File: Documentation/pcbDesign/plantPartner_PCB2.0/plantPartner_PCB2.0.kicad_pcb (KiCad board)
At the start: 2 copper layers, 85.3 x 70.5 mm, 60 parts, among them IC1 MPM3610, J1 Conn_01x04, J10 Screw_Terminal_01x02, J11 Conn_01x02, J16 Conn_01x04, J17 Conn_01x03, J2 Conn_01x04, J20 Conn_02x04_Top_Bottom, J21 Conn_01x04, J22 Conn_01x04, J23 Conn_01x01, J24 Conn_01x03, J25 Conn_01x03, J26 Conn_01x01, J27 Conn_01x01, J28 Conn_01x01, J29 Conn_01x02, J3 Conn_01x04, J30 Screw_Terminal_01x02, J4 Screw_Terminal, J5 Conn_01x02, J6 Barrel_Jack, J7 Screw_Terminal_01x02, J8 Conn_02x04_Top_Bottom, J9 Screw_Terminal_01x02, Q1 AO3400A, Q2 AO3400A, Q4 AO3400A, U2 MAX485, U3 ESP32-DEVKIT-V1

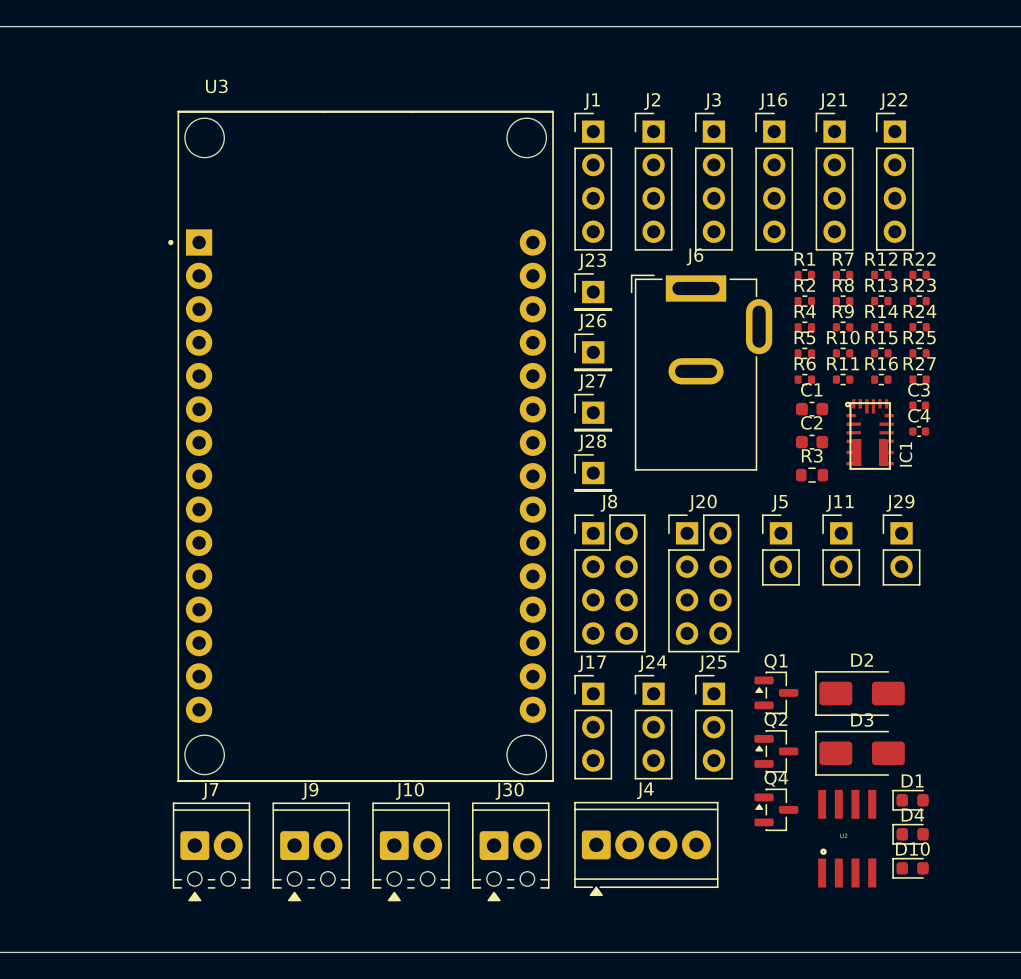
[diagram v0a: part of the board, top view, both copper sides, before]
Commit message: Cleaning up MOSFET circuits
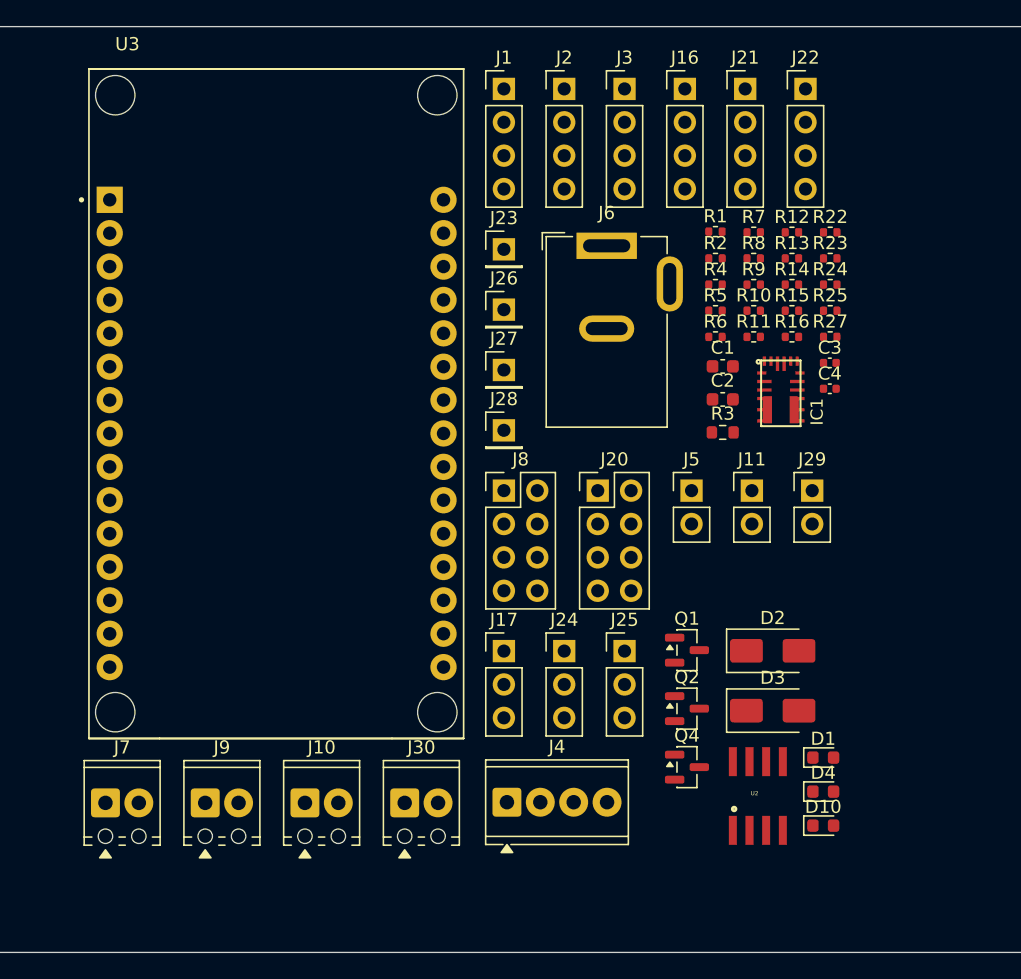
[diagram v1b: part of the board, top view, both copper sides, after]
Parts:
- moved R1 7.56 mm to (131.5, 50.4)
- moved U3 7.54 mm to (98.1, 63.5)
- moved C1 7.54 mm to (132.0, 60.7)
- moved C2 7.54 mm to (132.0, 63.2)
- moved C3 7.54 mm to (140.2, 60.4)
- moved C4 7.54 mm to (140.2, 62.4)
- moved D1 7.54 mm to (139.7, 90.4)
- moved D10 7.54 mm to (139.7, 95.6)
- moved D2 7.54 mm to (135.8, 82.3)
- moved D3 7.54 mm to (135.8, 86.8)
- moved D4 7.54 mm to (139.7, 93.0)
- moved IC1 7.54 mm to (136.4, 62.7)
- moved J11 7.54 mm to (134.2, 70.1)
- moved J16 7.54 mm to (129.1, 39.5)
- moved J20 7.54 mm to (122.5, 70.1)
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
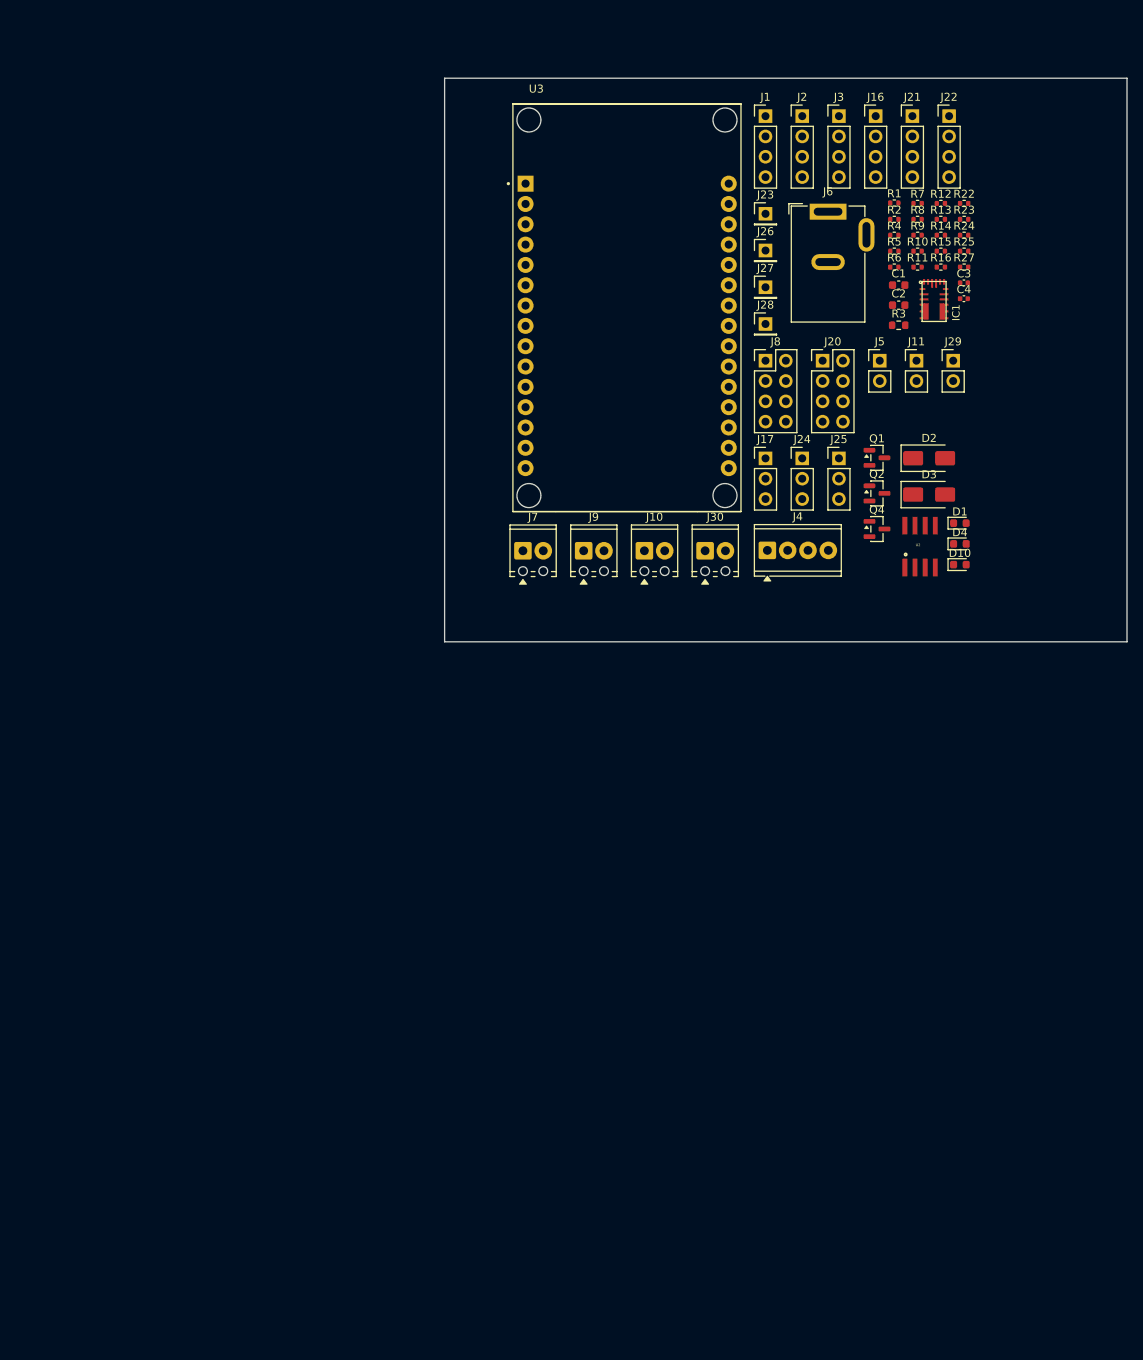
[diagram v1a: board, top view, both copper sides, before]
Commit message: I still need to test MOSFET circuits in Ltspice but I cleaned up the v2 Schematic and starting routing v2 PCB
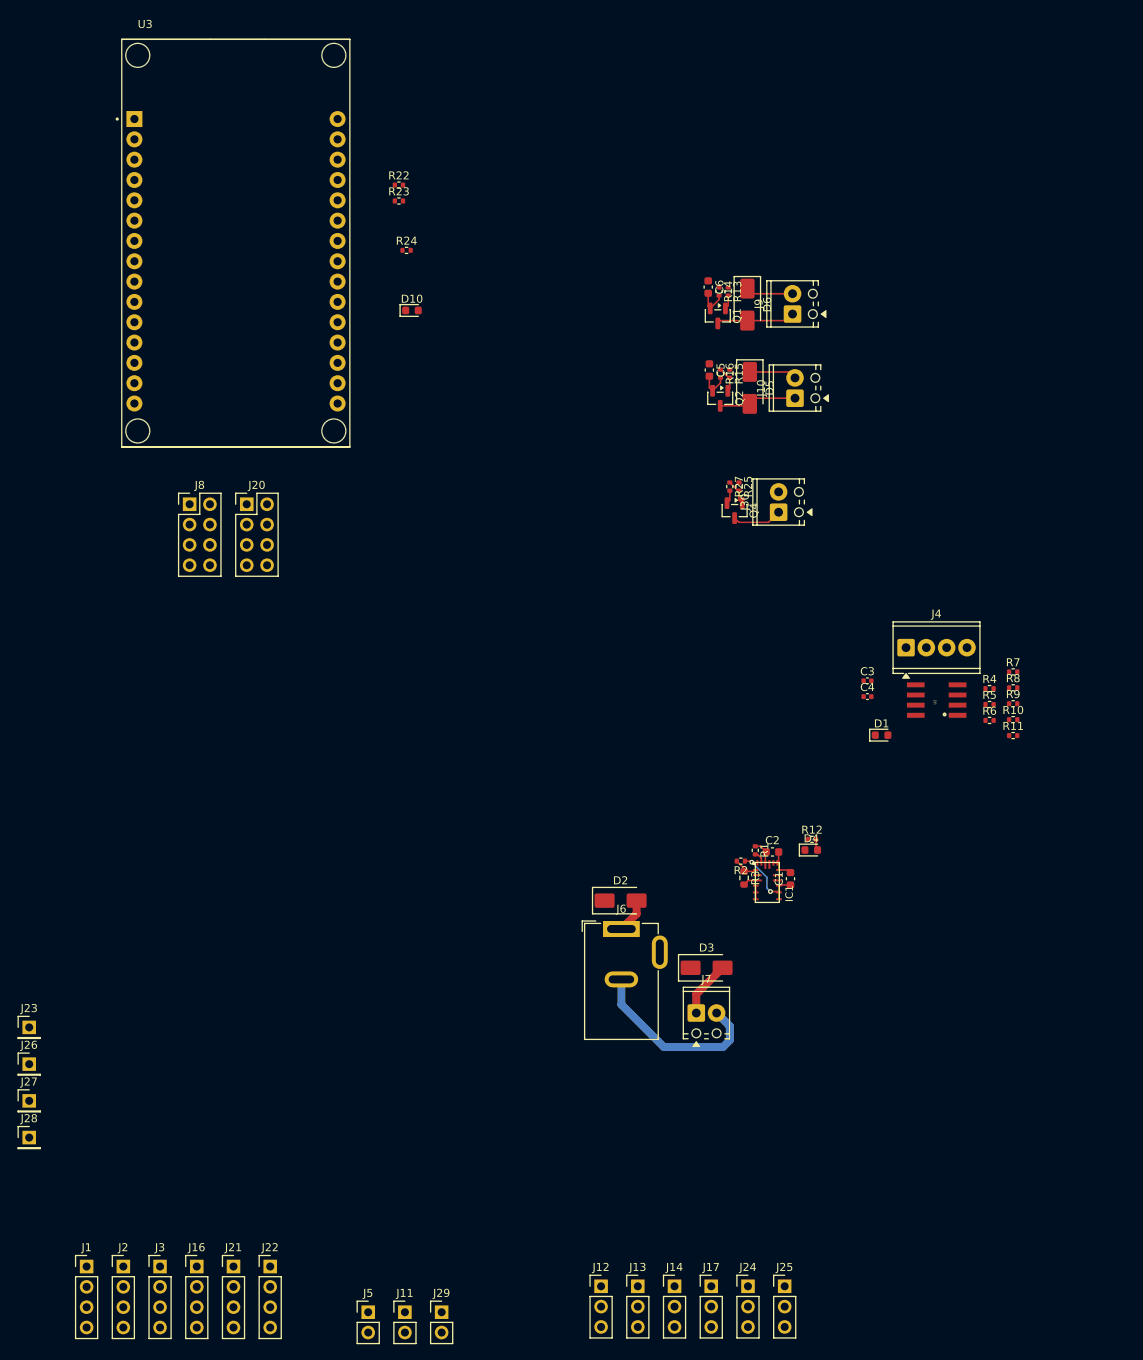
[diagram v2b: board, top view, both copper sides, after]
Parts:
- added C5: 220uF, Capacitor_SMD:C_0603_1608Metric, F.Cu at (108.3, 71.3)
- added C6: 220uF, Capacitor_SMD:C_0603_1608Metric, F.Cu at (108.2, 60.9)
- added D5: SS14, Diode_SMD:D_SMA, F.Cu at (113.4, 73.5)
- added D6: SS14, Diode_SMD:D_SMA, F.Cu at (113.1, 63.1)
- added J12: Conn_01x03, Connector_PinHeader_2.54mm:PinHeader_1x03_P2.54mm_Vertical, F.Cu at (94.8, 185.8)
- added J13: Conn_01x03, Connector_PinHeader_2.54mm:PinHeader_1x03_P2.54mm_Vertical, F.Cu at (99.4, 185.8)
- added J14: Conn_01x03, Connector_PinHeader_2.54mm:PinHeader_1x03_P2.54mm_Vertical, F.Cu at (104.0, 185.8)
- moved J1 167.0 mm to (30.5, 183.3)
- moved J16 167.0 mm to (44.3, 183.3)
- moved J2 167.0 mm to (35.1, 183.3)
- moved J21 167.0 mm to (48.9, 183.3)
- moved J22 167.0 mm to (53.5, 183.3)
- moved J3 167.0 mm to (39.7, 183.3)
- moved J23 137.2 mm to (23.3, 153.5)
- moved J26 137.2 mm to (23.3, 158.0)
- moved J27 137.2 mm to (23.3, 162.6)
- moved J28 137.2 mm to (23.3, 167.2)
- moved J5 135.0 mm to (65.7, 189.1)
- moved J11 135.0 mm to (70.3, 189.1)
- moved J29 135.0 mm to (74.9, 189.1)
- moved J17 103.7 mm to (108.6, 185.8)
- moved J24 103.7 mm to (113.2, 185.8)
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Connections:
- J10 pad 1: /Drain -> /F_Drain
- J10 pad 2: +12V -> +5V
- J30 pad 1: /Drain -> /L_Drain
- J9 pad 1: /Drain -> /W_Drain
- J9 pad 2: +12V -> +5V
- Q1 pad 1: /Gate -> /W_Gate
- Q1 pad 3: /Drain -> /W_Drain
- Q2 pad 1: /Gate -> /F_Gate
- Q2 pad 3: /Drain -> /F_Drain
- Q4 pad 1: /Gate -> /L_Gate
- Q4 pad 3: /Drain -> /L_Drain
- R13 pad 2: /Gate -> /W_Gate
- R14 pad 1: /Gate -> /W_Gate
- R15 pad 2: /Gate -> /F_Gate
- R16 pad 1: /Gate -> /F_Gate
- R25 pad 2: /Gate -> /L_Gate
- R27 pad 1: /Gate -> /L_Gate
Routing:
- net GND: track 0.00 -> 39.5 mm
- net +5V: track 0.00 -> 21.5 mm, vias 0 -> 2
- net /W_Drain: track 0.00 -> 9.83 mm
- net /F_Drain: track 0.00 -> 9.74 mm
- net /12V_SCREW: track 0.00 -> 7.01 mm
- net /L_Drain: track 0.00 -> 6.24 mm
- net /12V_JACK: track 0.00 -> 4.34 mm
- net /F_Gate: track 0.00 -> 3.31 mm
- net /L_Gate: track 0.00 -> 3.29 mm
- net +12V: track 0.00 -> 3.28 mm
- net /FB: track 0.00 -> 3.18 mm
- net /W_Gate: track 0.00 -> 1.75 mm
- net /SW: track 0.00 -> 1.70 mm
- net /EN: track 0.00 -> 1.53 mm
- net Net-(D4-A): track 0.00 -> 1.41 mm
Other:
- board outline removed

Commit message: Routed v2 PCB some more. Finished routing power sources, Buck Converter, MOSFET circuits, and most of RS485 Transceiver. I forgot about KiCad but will not next time I get a big chunk of time
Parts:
- removed J16: Conn_01x04, Connector_PinHeader_2.54mm:PinHeader_1x04_P2.54mm_Vertical
- added J15: Conn_01x03, Connector_PinHeader_2.54mm:PinHeader_1x03_P2.54mm_Vertical, F.Cu at (95.0, 128.6)
- J4: value Screw_Terminal -> Screw_Terminal_01x04
- moved J27 239.4 mm to (256.1, 106.7)
- moved J26 236.1 mm to (255.9, 117.6)
- moved J13 180.0 mm to (259.9, 104.2)
- moved J12 177.6 mm to (259.8, 120.3), turned to 180 degrees
- moved J22 175.5 mm to (218.2, 123.0)
- moved J21 174.2 mm to (217.4, 139.5)
- moved J5 171.1 mm to (217.5, 110.0)
- moved D6 163.8 mm to (267.5, 117.6)
- moved Q1 163.8 mm to (263.9, 119.0)
- moved C6 163.8 mm to (262.6, 115.4)
- moved J9 163.8 mm to (273.2, 118.8)
- moved R13 163.8 mm to (265.1, 116.0)
- moved R14 163.8 mm to (264.0, 116.0)
- moved C5 157.7 mm to (262.6, 104.4)
- moved Q2 157.7 mm to (263.9, 108.0)
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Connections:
- J1 pad 1: /EN -> +12V
- J1 pad 2: +12V -> /EN
- J4 pad 1: /B -> GND
- J4 pad 3: +12V -> /B
- J4 pad 4: GND -> +12V
- R11 pad 1: /B -> /A
- R11 pad 2: /A -> /B
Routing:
- net GND: track 39.5 -> 81.3 mm, vias 0 -> 3
- net +5V: track 21.5 -> 45.2 mm, vias 2 -> 3
- net +12V: track 3.28 -> 24.7 mm
- net /DE: track 0.00 -> 12.8 mm
- net /FB: track 3.18 -> 15.7 mm, vias 0 -> 1
- net /A: track 0.00 -> 9.39 mm
- net /B: track 0.00 -> 9.21 mm
- net /DI: track 0.00 -> 6.33 mm
- net /RO: track 0.00 -> 6.16 mm
- net /EN: track 1.53 -> 6.57 mm
- net Net-(D10-A): track 0.00 -> 1.45 mm
- net Net-(D1-A): track 0.00 -> 1.44 mm
- net /12V_SCREW: track 7.01 -> 5.94 mm
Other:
- board text added: "Ready to be placed"
